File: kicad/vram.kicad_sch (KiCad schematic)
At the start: 11 parts, among them U110 74LS273, U122 74LS273, U124 74F257, U125 74F257, U72 TMS4416, U73 TMS4416, U82 74LS00, U96 74F257N, U97 74F257N

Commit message: update kicad project
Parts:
- added C82, C83: C_Bypass_5mm, seequa_footprints:C_Seequa_Bypass_Film_5mm, symbol seequa:C_Bypass_Film_2.54mm
- added U117: 74F04, Package_DIP:DIP-14_W7.62mm, symbol 74xx:74LS04
- added U67: 74LS374, Package_DIP:DIP-20_W7.62mm, symbol 74xx:74LS374
- added U68: 74LS244, Package_DIP:DIP-20_W7.62mm, symbol 74xx:74LS244
- RN14: seq_coord (none) -> E18; seq_silkscreen RN6 -> (none)
- RN15: renamed from RN3; seq_coord (none) -> E17
- U110: seq_coord (none) -> E19; seq_notes CC Latch -> AT Latch
- U122: seq_coord (none) -> I19; seq_notes AT Latch -> CC Latch
- U124: seq_coord (none) -> J12
- U125: seq_coord (none) -> J14
- U72: seq_coord (none) -> D17; seq_silkscreen (none) -> TMS4416
- U73: seq_coord (none) -> D18; seq_silkscreen (none) -> TMS4416
- U82: seq_coord (none) -> D20; seq_silkscreen (none) -> LS00
- U96: seq_coord (none) -> L12; seq_silkscreen (none) -> F257
- U97: seq_coord (none) -> L14; seq_silkscreen (none) -> F257
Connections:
- net ~{VM_{WR}} is gone; now on net ~{VM_{WR_T}}: RN15.9 (R6.2)
- net +5V: now also C82.1, C83.1, U67.20 (VCC), U68.20 (VCC)
- net AT_D2: now also U110.5 (Q1); no longer U110.12 (Q4)
- net AT_D3: now also U110.2 (Q0); no longer U110.5 (Q1)
- net AT_D7: now also U110.12 (Q4); no longer U110.2 (Q0)
- net CC_D2: now also U122.5 (Q1); no longer U122.12 (Q4)
- net CC_D3: now also U122.2 (Q0); no longer U122.5 (Q1)
- net CC_D5: now also U122.12 (Q4); no longer U122.16 (Q6)
- net CC_D7: now also U122.16 (Q6); no longer U122.2 (Q0)
- net GND: now also C82.2, C83.2, U67.10 (GND), U68.10 (GND)
- net VD0: now also U67.4 (D1), U68.5 (O2b)
- net VD1: now also U67.3 (D0), U68.3 (O3b)
- net VD2: now also U67.14 (D5), U68.7 (O1b)
- net VD3: now also U67.8 (D3), U68.9 (O0b)
- net VD4: now also U67.13 (D4), U68.12 (O3a)
- net VD5: now also U67.7 (D2), U68.14 (O2a)
- net VD6: now also U67.17 (D6), U68.16 (O1a)
- net VD7: now also U67.18 (D7), U68.18 (O0a)
- net ~{VM_{CAS_T}}: now also RN15.8 (R7.2); no longer RN15.7 (R7.1)
- net ~{VM_{CAS}}: now also RN15.7 (R7.1); no longer RN15.8 (R7.2)
- net ~{VM_{RAS_T}}: now also RN15.10 (R5.2); no longer RN15.5 (R5.1), U72.5 (~{RAS}), U73.5 (~{RAS}), U82.1, U82.2
- net ~{VM_{RAS}}: now also RN15.5 (R5.1), U72.5 (~{RAS}), U73.5 (~{RAS}), U82.1, U82.2; no longer RN15.10 (R5.2)
- net ~{VM_{WR_T}}: now reaches RN15.6 (R6.1), U72.4 (~{WE}), U73.4 (~{WE})
- net ~{VM_{WR_T}}: now also U68.1 (OEa), U68.19 (OEb)
- net CRM_P21: now reaches U122.11 (Cp)
- net CRM_{VA5} renamed CRM_{A12}
- net MA0 renamed CRT_{A0}
- net MA1 renamed CRT_{A1}
- net MA10 renamed CRT_{A10}
- net MA11 renamed CRT_{A11}
- net MA2 renamed CRT_{A2}
- net MA3 renamed CRT_{A3}
- net MA4 renamed CRT_{A4}
- net MA5 renamed CRT_{A5}
- net MA6 renamed CRT_{A6}
- net MA7 renamed CRT_{A7}
- net MA8 renamed CRT_{A8}
- net MA9 renamed CRT_{A9}
- net VA0 renamed VMA0
- net VA0_{t} renamed VMA0_{t}
- net VA1 renamed VMA1
- net VA1_{t} renamed VMA1_{t}
- net VA2 renamed VMA2
- net VA2_{t} renamed VMA2_{t}
- net VA3 renamed VMA3
- net VA3_{t} renamed VMA3_{t}
- net VA4 renamed VMA4
- net VA4_{t} renamed VMA4_{t}
- net VA5 renamed VMA5
- net VA5_{t} renamed VMA5_{t}
- net VA6 renamed VMA6
- net VA6_{t} renamed VMA6_{t}
- net VA7 renamed VMA7
- net VA7_{t} renamed VMA7_{t}
- net XA0 renamed CPU_{A0}
- net XA1 renamed CPU_{A1}
- net XA10 renamed CPU_{A10}
- net XA11 renamed CPU_{A11}
- net XA12 renamed CPU_{A12}
- net XA13 renamed CPU_{A13}
- net XA2 renamed CPU_{A2}
- net XA3 renamed CPU_{A3}
- net XA4 renamed CPU_{A4}
- net XA5 renamed CPU_{A5}
- net XA6 renamed CPU_{A6}
- net XA7 renamed CPU_{A7}
- net XA8 renamed CPU_{A8}
- net XA9 renamed CPU_{A9}
- net ~{MUX_IN_{A}} renamed CRM_{A13}
- new net VM_{RDGATE}: U117.10, U67.11 (Cp)
- new net XD0: U67.5 (O1), U68.15 (I2b)
- new net XD1: U67.2 (O0), U68.17 (I3b)
- new net XD2: U67.15 (O5), U68.13 (I1b)
- new net XD3: U67.9 (O3), U68.11 (I0b)
- new net XD4: U67.12 (O4), U68.8 (I3a)
- new net XD5: U67.6 (O2), U68.6 (I2a)
- new net XD6: U67.16 (O6), U68.4 (I1a)
- new net XD7: U67.19 (O7), U68.2 (I0a)
- new net ~{VM_{RDGATE}}: U117.11
- new net ~{VRAM_{RD}}: U67.1 (OE)
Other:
- moved on the sheet: RN15, U72, U73, U82A, U82B

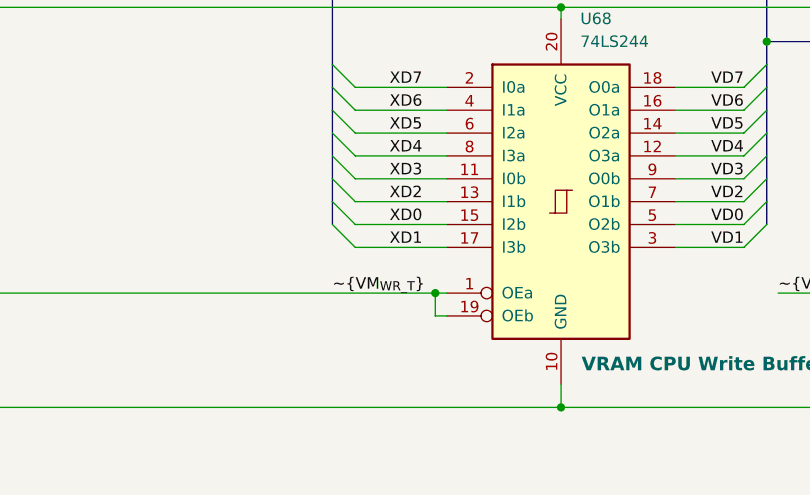
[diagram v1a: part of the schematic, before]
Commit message: Add parallel port, game port
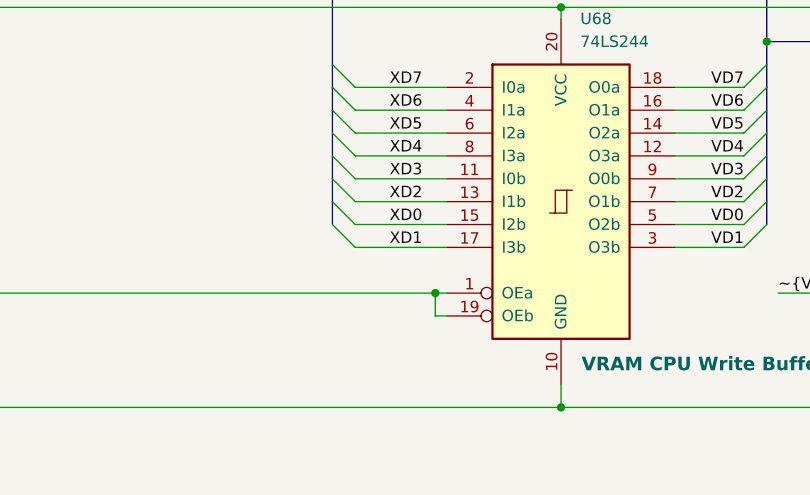
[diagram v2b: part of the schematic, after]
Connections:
- net ~{VM_{WR_T}}: no longer RN15.6 (R6.1), U68.1 (OEa), U68.19 (OEb)
- new net ~{VM_{WR}}: RN15.6 (R6.1), U68.1 (OEa), U68.19 (OEb)
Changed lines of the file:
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@@
-		)
-	)
-	(label "~{VM_{WR_T}}"
-		(at 80.01 252.73 0)
-		(effects
-			(font
-				(size 1.27 1.27)
-			)
-			(justify left bottom)
 		)
 	)

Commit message: Updates, chameleon logo
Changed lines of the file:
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@@
 	(wire
 		(pts
+			(xy 134.62 252.73) (xy 139.7 252.73)
+		)
+		(stroke
+			(width 0)
+			(type default)
+		)
+	)
+	(wire
+		(pts
 			(xy 121.92 81.28) (xy 13.97 81.28)
 		)
@@
 	(wire
 		(pts
+			(xy 134.62 213.36) (xy 134.62 252.73)
+		)
+		(stroke
+			(width 0)
+			(type default)
+		)
+	)
+	(wire
+		(pts
 			(xy 251.46 157.48) (xy 208.28 157.48)
 		)
@@
 	(wire
 		(pts
-			(xy 129.54 252.73) (xy 139.7 252.73)
+			(xy 26.67 213.36) (xy 134.62 213.36)
 		)
 		(stroke
@@
 		)
 	)
-	(label "~{VM_{RDGATE}}"
-		(at 129.54 252.73 0)
-		(effects
-			(font
-				(size 1.27 1.27)
-			)
-			(justify left bottom)
-		)
-	)
 	(label "VMA0_{t}"
 		(at 345.44 39.37 180)
@@
 		)
 	)
+	(hierarchical_label "~{VM_{RDGATE}}"
+		(shape input)
+		(at 26.67 213.36 180)
+		(effects
+			(font
+				(size 1.27 1.27)
+			)
+			(justify right)
+		)
+	)
